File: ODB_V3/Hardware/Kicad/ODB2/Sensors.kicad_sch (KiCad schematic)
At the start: 24 parts, among them J4 RF2-04A-T-00-50-G, U10 ADXL382-2BCCZ-RL7, U4 MS580301BA01-00, U5 L76L-M33, U6 BNO055, U9 MAX6612MXK

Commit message: fix: labels
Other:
- note removed: "Address I2C = 0x1D"
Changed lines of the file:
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@@
 	(text "Max consumption 0.52mA"
 		(exclude_from_sim no)
-		(at 107.95 118.11 0)
+		(at 107.442 118.11 0)
 		(effects
 			(font
@@
 	(text "Temperature Sensor"
 		(exclude_from_sim no)
-		(at 161.798 30.48 0)
+		(at 171.196 30.734 0)
 		(effects
 			(font
-				(size 1.27 1.27)
+				(size 2.54 2.54)
 				(thickness 0.254)
 				(bold yes)
@@
 		)
 	)
-	(text "Address I2C = 0x1D"
-		(exclude_from_sim no)
-		(at 24.892 166.624 0)
-		(effects
-			(font
-				(size 1.27 1.27)
-				(thickness 0.254)
-				(bold yes)
-			)
-		)
-	)
 	(text "Intégration pour antenne active"
 		(exclude_from_sim no)
@@
 	(text "Sensors"
 		(exclude_from_sim no)
-		(at 30.988 17.272 0)
+		(at 24.638 16.256 0)
 		(effects
 			(font
-				(size 6 6)
+				(size 4.064 4.064)
 				(thickness 0.254)
 				(bold yes)
@@
 	(text "Acceleromter High G"
 		(exclude_from_sim no)
-		(at 24.892 118.11 0)
+		(at 34.544 118.872 0)
 		(effects
 			(font
-				(size 1.27 1.27)
+				(size 2.54 2.54)
 				(thickness 0.254)
 				(bold yes)
@@
 	(text "Barometer"
 		(exclude_from_sim no)
-		(at 19.812 87.376 0)
+		(at 24.384 87.884 0)
 		(effects
 			(font
-				(size 1.27 1.27)
+				(size 2.54 2.54)
 				(thickness 0.254)
 				(bold yes)
@@
 	(text "IMU Low G"
 		(exclude_from_sim no)
-		(at 14.732 30.226 0)
+		(at 14.732 31.75 0)
 		(effects
 			(font
-				(size 1.27 1.27)
+				(size 2.54 2.54)
 				(thickness 0.254)
 				(bold yes)
@@
 	(wire
 		(pts
+			(xy 35.56 125.73) (xy 35.56 127)
+		)
+		(stroke
+			(width 0)
+			(type default)
+		)
+	)
+	(wire
+		(pts
 			(xy 246.38 129.54) (xy 250.19 129.54)
 		)
@@
 	(wire
 		(pts
-			(xy 35.56 124.46) (xy 35.56 127)
-		)
-		(stroke
-			(width 0)
-			(type default)
-		)
-	)
-	(wire
-		(pts
 			(xy 110.49 160.02) (xy 101.6 160.02)
 		)
@@
 	(symbol
 		(lib_id "power:+3V3")
-		(at 35.56 124.46 0)
+		(at 35.56 125.73 0)
 		(unit 1)
 		(exclude_from_sim no)
@@
 		(dnp no)
 		(property "Reference" "#PWR088"
-			(at 35.56 128.27 0)
+			(at 35.56 129.54 0)
 			(effects
 				(font
@@
 		)
 		(property "Value" "+3V3"
-			(at 35.56 120.65 0)
+			(at 35.56 121.92 0)
 			(effects
 				(font
@@
 		)
 		(property "Footprint" ""
-			(at 35.56 124.46 0)
+			(at 35.56 125.73 0)
 			(effects
 				(font
@@
 		)
 		(property "Datasheet" ""
-			(at 35.56 124.46 0)
+			(at 35.56 125.73 0)
 			(effects
 				(font
@@
 		)
 		(property "Description" "Power symbol creates a global label with name \"+3V3\""
-			(at 35.56 124.46 0)
+			(at 35.56 125.73 0)
 			(effects
 				(font

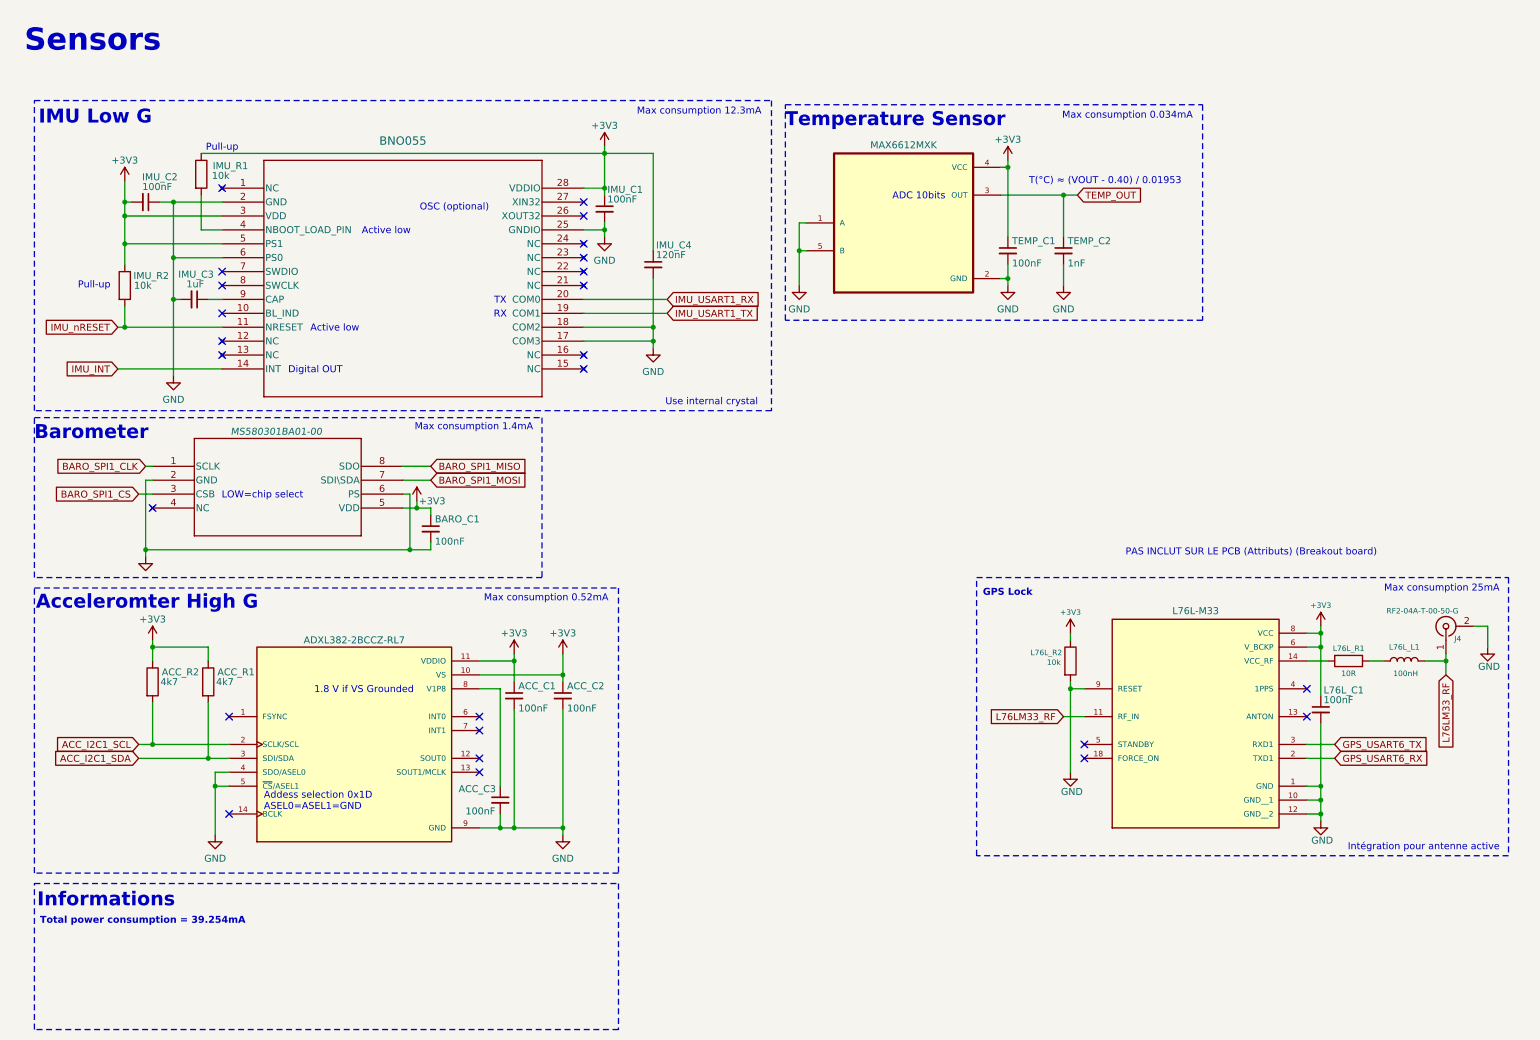
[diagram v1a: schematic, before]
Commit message: feat: add all missing pins on stm32cubeide and kicad + add extend connectivities (UART3, SPI2)
Missing Pinout:
IMU_INT
TEMP_OUT
GPS_FUNCT_X
BUZZER_PWM
VIN_An
Senses_X
Fire_X
Pyro_Arm
PA_An
5V_An
3V3_An
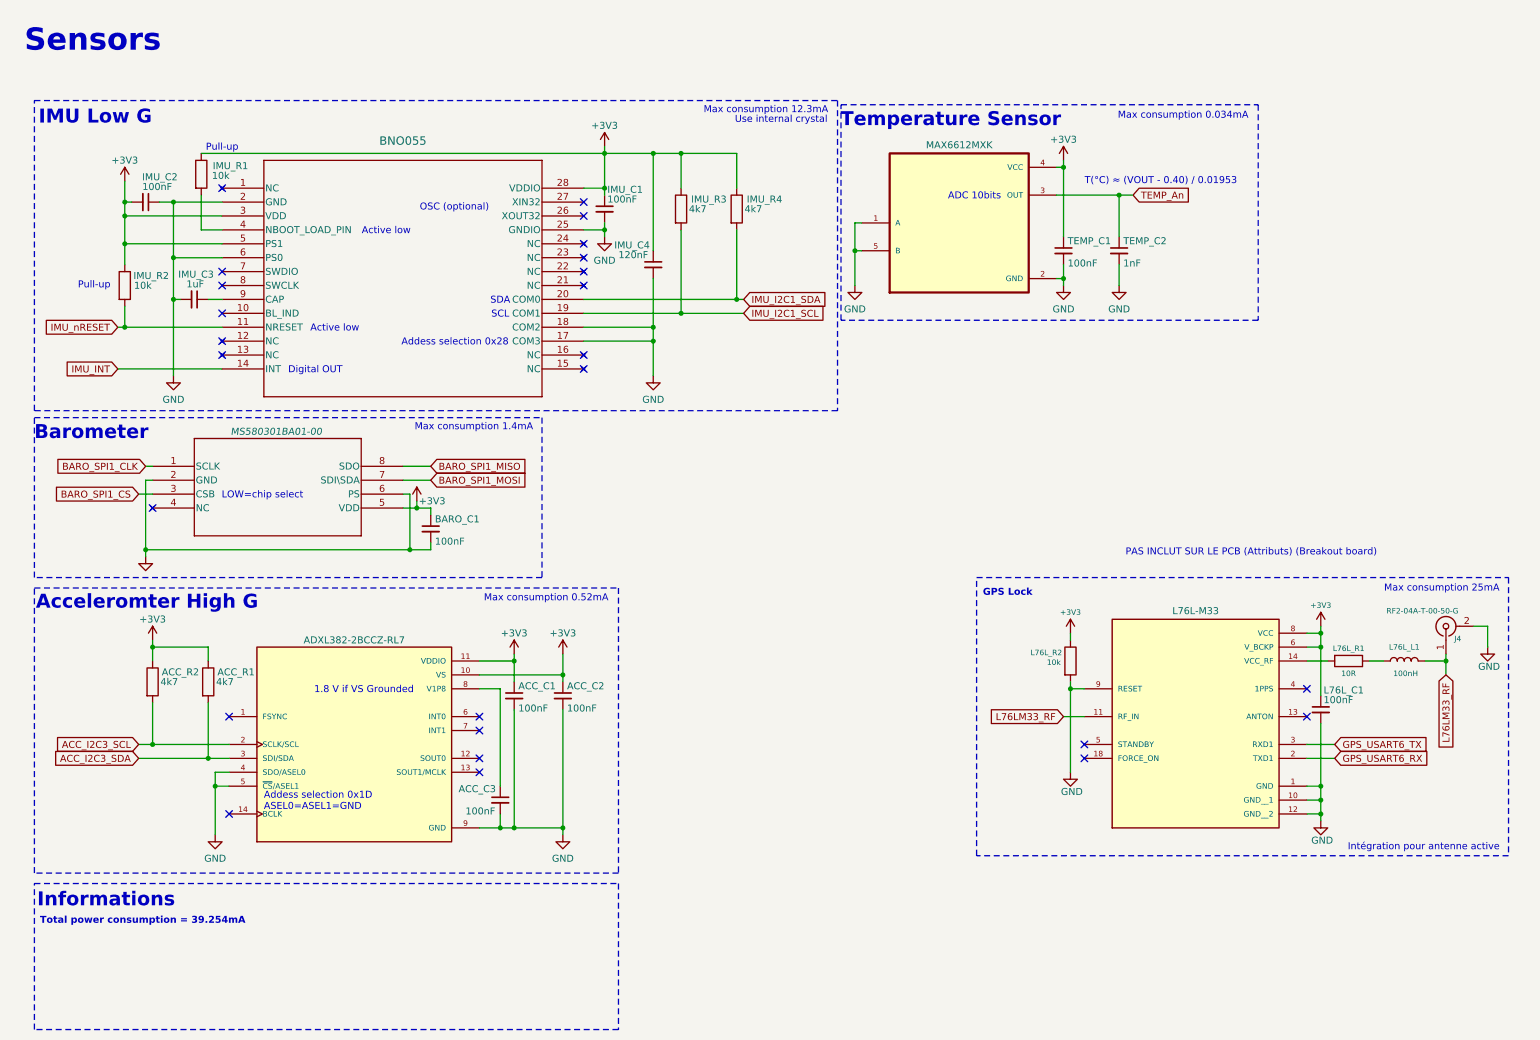
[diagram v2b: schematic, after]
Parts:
- added IMU_R3, IMU_R4: 4k7, Resistor_SMD:R_0603_1608Metric, symbol Device:R
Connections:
- net +3V3: now also IMU_R3.1, IMU_R4.1
- net ACC_I2C1_SCL renamed ACC_I2C3_SCL
- net ACC_I2C1_SDA renamed ACC_I2C3_SDA
- net IMU_USART1_RX renamed IMU_I2C1_SDA
- net IMU_I2C1_SDA: now also IMU_R4.2
- net IMU_USART1_TX renamed IMU_I2C1_SCL
- net IMU_I2C1_SCL: now also IMU_R3.2
- net TEMP_OUT renamed TEMP_An
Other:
- note added: "Addess selection 0x28"
- note added: "SCL"
- note added: "SDA"
- note removed: "RX"
- note removed: "TX"
- moved on the sheet: TEMP_C1, TEMP_C2

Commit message: fix: change component attributs
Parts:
- J4, L76L_C1, L76L_L1, L76L_R1, L76L_R2, U5: now left out of the parts list
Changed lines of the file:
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@@
 		(unit 1)
 		(exclude_from_sim no)
-		(in_bom yes)
-		(on_board yes)
+		(in_bom no)
+		(on_board no)
 		(dnp no)
 		(property "Reference" "U5"
@@
 		(unit 1)
 		(exclude_from_sim no)
-		(in_bom yes)
-		(on_board yes)
+		(in_bom no)
+		(on_board no)
 		(dnp no)
 		(property "Reference" "#PWR049"
@@
 		(unit 1)
 		(exclude_from_sim no)
-		(in_bom yes)
-		(on_board yes)
+		(in_bom no)
+		(on_board no)
 		(dnp no)
 		(property "Reference" "L76L_R2"
@@
 		(unit 1)
 		(exclude_from_sim no)
-		(in_bom yes)
-		(on_board yes)
+		(in_bom no)
+		(on_board no)
 		(dnp no)
 		(property "Reference" "L76L_R1"
@@
 		(unit 1)
 		(exclude_from_sim no)
-		(in_bom yes)
-		(on_board yes)
+		(in_bom no)
+		(on_board no)
 		(dnp no)
 		(property "Reference" "#PWR060"
@@
 		(unit 1)
 		(exclude_from_sim no)
-		(in_bom yes)
-		(on_board yes)
+		(in_bom no)
+		(on_board no)
 		(dnp no)
 		(property "Reference" "#PWR048"
@@
 		(unit 1)
 		(exclude_from_sim no)
-		(in_bom yes)
-		(on_board yes)
+		(in_bom no)
+		(on_board no)
 		(dnp no)
 		(property "Reference" "#PWR061"
@@
 		(unit 1)
 		(exclude_from_sim no)
-		(in_bom yes)
-		(on_board yes)
+		(in_bom no)
+		(on_board no)
 		(dnp no)
 		(property "Reference" "#PWR052"
@@
 		(unit 1)
 		(exclude_from_sim no)
-		(in_bom yes)
-		(on_board yes)
+		(in_bom no)
+		(on_board no)
 		(dnp no)
 		(property "Reference" "J4"
@@
 		(unit 1)
 		(exclude_from_sim no)
-		(in_bom yes)
-		(on_board yes)
+		(in_bom no)
+		(on_board no)
 		(dnp no)
 		(property "Reference" "L76L_L1"
@@
 		(unit 1)
 		(exclude_from_sim no)
-		(in_bom yes)
-		(on_board yes)
+		(in_bom no)
+		(on_board no)
 		(dnp no)
 		(property "Reference" "L76L_C1"

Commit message: fix: some footprints/symboles link + add criticalLed pin
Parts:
- U10: footprint ADXL382-2BCCZ-RL7:XDCR_ADXL382-2BCCZ-RL7 -> ODB:XDCR_ADXL382-2BCCZ-RL7
- U4: footprint MS5803-01BA01_TEC -> ODB:MS5803-01BA01_TEC
- U5: footprint L76L-M33:XCVR_L76L-M33 -> ODB:XCVR_L76L-M33
- U6: footprint QFN_BNO055_BOS -> ODB:QFN_BNO055_BOS
- U9: footprint MAX6612MXK:SOT65P210X110-5N -> ODB:SOT65P210X110-5N
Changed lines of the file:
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@@
 			)
 		)
-		(property "Footprint" "MS5803-01BA01_TEC"
+		(property "Footprint" "ODB:MS5803-01BA01_TEC"
 			(at 58.674 81.534 0)
 			(effects
@@
 			)
 		)
-		(property "Footprint" "L76L-M33:XCVR_L76L-M33"
+		(property "Footprint" "ODB:XCVR_L76L-M33"
 			(at 226.06 139.7 0)
 			(effects
@@
 			)
 		)
-		(property "Footprint" "ADXL382-2BCCZ-RL7:XDCR_ADXL382-2BCCZ-RL7"
+		(property "Footprint" "ODB:XDCR_ADXL382-2BCCZ-RL7"
 			(at 72.39 144.78 0)
 			(effects
@@
 			)
 		)
-		(property "Footprint" "QFN_BNO055_BOS"
+		(property "Footprint" "ODB:QFN_BNO055_BOS"
 			(at 48.26 43.18 0)
 			(effects
@@
 			)
 		)
-		(property "Footprint" "MAX6612MXK:SOT65P210X110-5N"
+		(property "Footprint" "ODB:SOT65P210X110-5N"
 			(at 182.88 49.53 0)
 			(effects

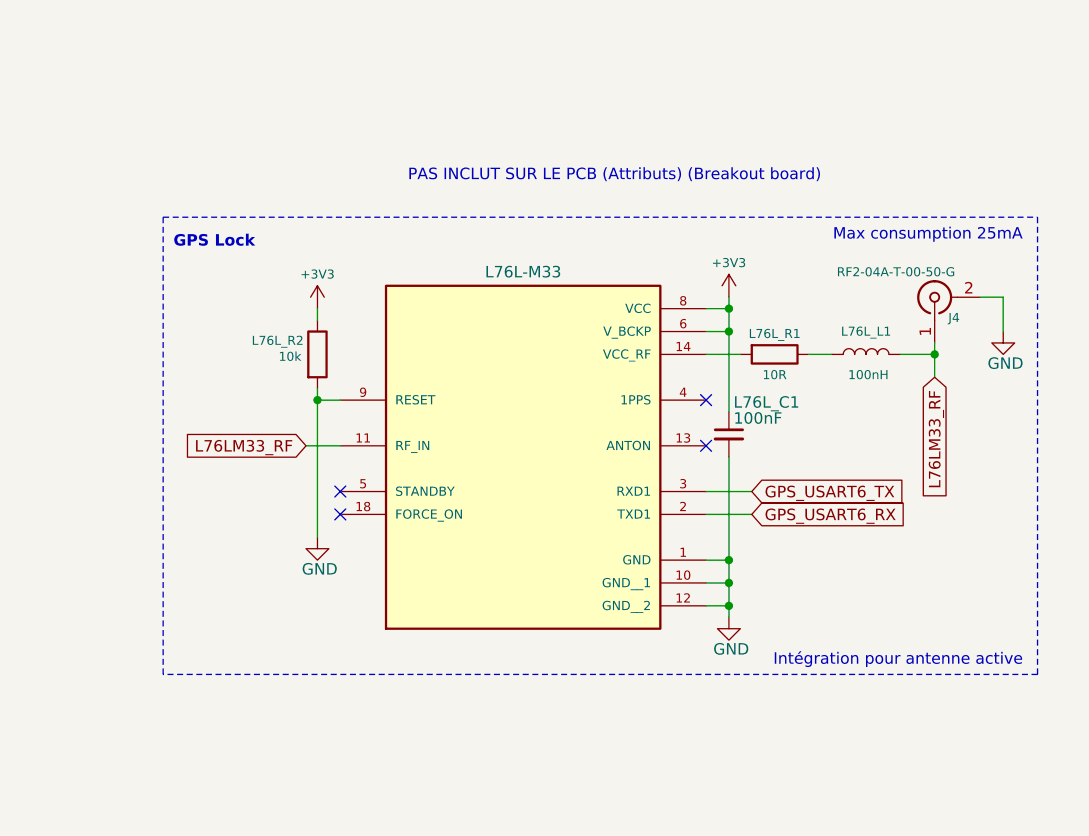
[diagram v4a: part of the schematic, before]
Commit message: wip (breakoutboard): l76lm33 schematic + start pcb
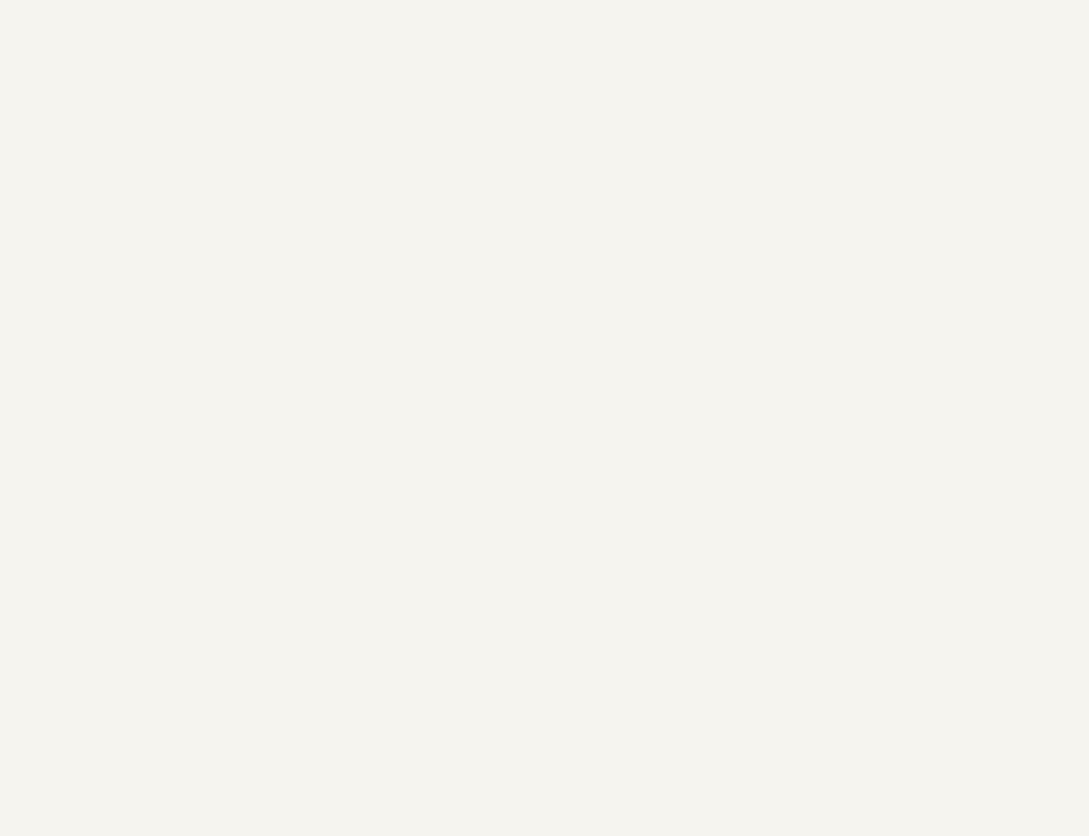
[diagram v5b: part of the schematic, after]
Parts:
- removed J4: RF2-04A-T-00-50-G, Connector_Coaxial:SMA_Wurth_60312002114503_Vertical, symbol Connector:Conn_Coaxial
- removed L76L_C1: 100nF, Capacitor_SMD:C_0603_1608Metric, symbol Device:C_Small
- removed L76L_L1: 100nH, Inductor_SMD:L_0603_1608Metric, symbol Device:L
- removed L76L_R1: 10R, Resistor_SMD:R_0603_1608Metric, symbol Device:R
- removed L76L_R2: 10k, Resistor_SMD:R_0603_1608Metric, symbol Device:R
- removed U5: L76L-M33, ODB:XCVR_L76L-M33, symbol ODB2:L76L-M33
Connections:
- no-connect marks 25 -> 21
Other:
- note removed: "GPS Lock"
- note removed: "Intégration pour antenne active"
- note removed: "Max consumption 25mA"
- note removed: "PAS INCLUT SUR LE PCB (Attributs) (Breakout board)"

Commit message: wip: route qspi
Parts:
- added BARO_R4: 22R, Resistor_SMD:R_0402_1005Metric, symbol Device:R
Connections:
- net BARO_SPI1_MISO: now also BARO_R4.1; no longer U4.8 (SDO)
- new net: BARO_R4.2, U4.8 (SDO)
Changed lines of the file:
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@@
 	(rectangle
 		(start 13.97 85.09)
-		(end 106.68 114.3)
+		(end 121.92 114.3)
 		(stroke
 			(width 0)
@@
 	(wire
 		(pts
+			(xy 90.17 93.98) (xy 91.44 93.98)
+		)
+		(stroke
+			(width 0)
+			(type default)
+		)
+	)
+	(wire
+		(pts
 			(xy 35.56 127) (xy 35.56 129.54)
 		)
@@
 	(wire
 		(pts
+			(xy 81.28 93.98) (xy 82.55 93.98)
+		)
+		(stroke
+			(width 0)
+			(type default)
+		)
+	)
+	(wire
+		(pts
 			(xy 99.06 157.48) (xy 99.06 160.02)
 		)
@@
 		(pts
 			(xy 110.49 160.02) (xy 101.6 160.02)
-		)
-		(stroke
-			(width 0)
-			(type default)
-		)
-	)
-	(wire
-		(pts
-			(xy 81.28 93.98) (xy 86.36 93.98)
 		)
 		(stroke
@@
 	(global_label "BARO_SPI1_MISO"
 		(shape input)
-		(at 86.36 93.98 0)
+		(at 91.44 93.98 0)
 		(fields_autoplaced yes)
 		(effects
@@
 		)
 		(property "Intersheetrefs" "${INTERSHEET_REFS}"
-			(at 105.1295 93.98 0)
+			(at 110.2095 93.98 0)
 			(effects
 				(font
@@
 					(unit 1)
 				)
+			)
+		)
+	)
+	(symbol
+		(lib_id "Device:R")
+		(at 86.36 93.98 270)
+		(unit 1)
+		(exclude_from_sim no)
+		(in_bom yes)
+		(on_board yes)
+		(dnp no)
+		(property "Reference" "BARO_R4"
+			(at 117.602 93.98 90)
+			(effects
+				(font
+					(size 1 1)
+				)
+			)
+		)
+		(property "Value" "22R"
+			(at 112.268 93.98 90)
+			(effects
+				(font
+					(size 1 1)
+				)
+			)
+		)
+		(property "Footprint" "Resistor_SMD:R_0402_1005Metric"
+			(at 86.36 92.202 90)
+			(effects
+				(font
+					(size 1 1)
+				)
+				(hide yes)
+			)
+		)
+		(property "Datasheet" "~"
+			(at 86.36 93.98 0)
+			(effects
+				(font
+					(size 1 1)
+				)
+				(hide yes)
+			)
+		)
+		(property "Description" ""
+			(at 86.36 93.98 0)
+			(effects
+				(font
+					(size 1.27 1.27)
+				)
+				(hide yes)
+			)
+		)
+		(pin "1"
+		)
+		(pin "2"
+		)
+		(instances
+			(project "ODB2"
+				(path "/4b06c5d1-aa8b-48ed-8972-b43a60cfab78/eac5f07f-d6a3-4c95-b286-7cebf46e30db"
+					(reference "BARO_R4")
+					(unit 1)
+				)

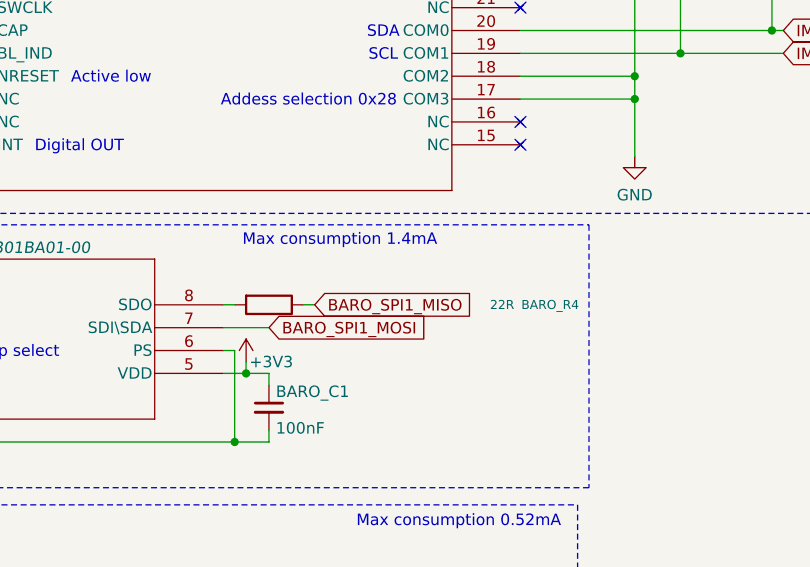
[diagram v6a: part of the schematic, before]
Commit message: wip: add testpads (todo) + add MISO sd resistance + fix pyro labels
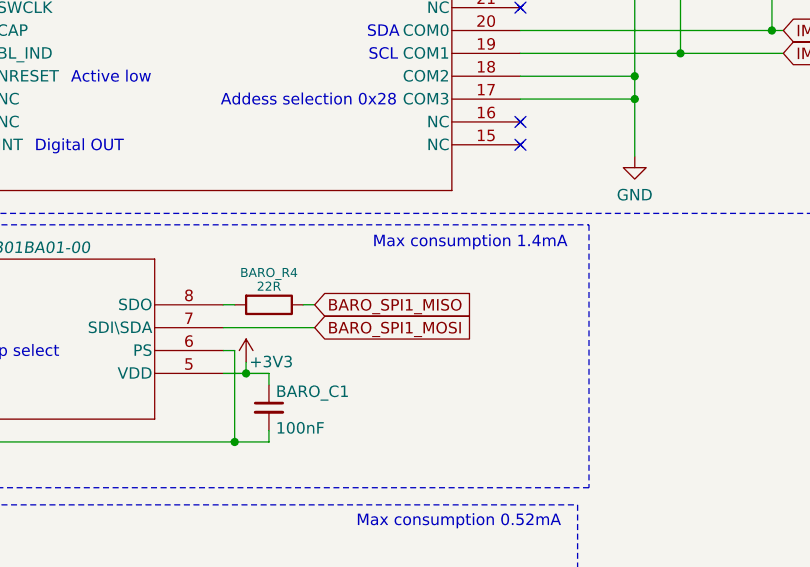
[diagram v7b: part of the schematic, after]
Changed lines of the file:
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@@
 	(text "Max consumption 1.4mA"
 		(exclude_from_sim no)
-		(at 94.234 86.868 0)
+		(at 108.712 87.122 0)
 		(effects
 			(font
@@
 	(wire
 		(pts
-			(xy 81.28 96.52) (xy 86.36 96.52)
+			(xy 81.28 96.52) (xy 91.44 96.52)
 		)
 		(stroke
@@
 	(global_label "BARO_SPI1_MOSI"
 		(shape input)
-		(at 86.36 96.52 0)
+		(at 91.44 96.52 0)
 		(fields_autoplaced yes)
 		(effects
@@
 		)
 		(property "Intersheetrefs" "${INTERSHEET_REFS}"
-			(at 105.1295 96.52 0)
+			(at 110.2095 96.52 0)
 			(effects
 				(font
@@
 		(dnp no)
 		(property "Reference" "BARO_R4"
-			(at 117.602 93.98 90)
+			(at 86.36 90.424 90)
 			(effects
 				(font
@@
 		)
 		(property "Value" "22R"
-			(at 112.268 93.98 90)
-			(effects
-				(font
+			(at 86.36 91.948 90)
+			(effects
+				(font

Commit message: fix : silkscreen DRC completely done
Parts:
- BARO_R4: footprint Resistor_SMD:R_0402_1005Metric -> ODB:R_0402_1005Metric
